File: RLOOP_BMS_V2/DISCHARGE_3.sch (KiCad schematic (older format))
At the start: 60 parts, among them Q2 PMV20ENR, Q3 PMV20ENR, Q4 PMV20ENR, Q5 PMV20ENR, Q6 PMV20ENR, Q7 PMV20ENR

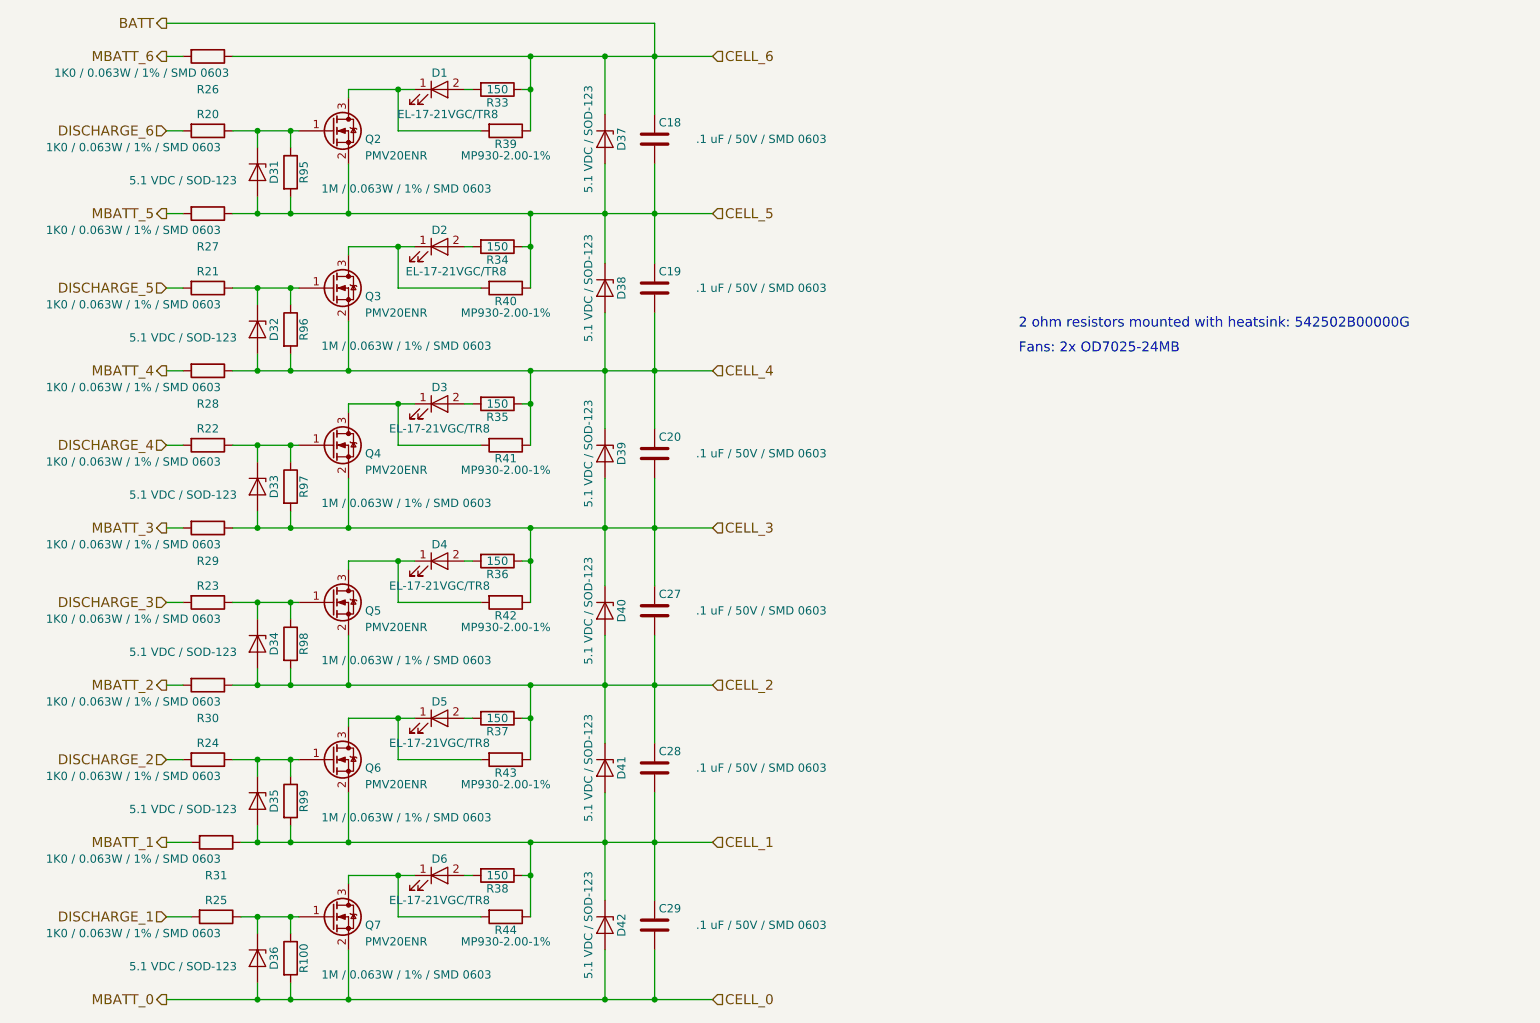
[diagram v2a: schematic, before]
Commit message: Added BOM, added pin 1 markings on a few parts
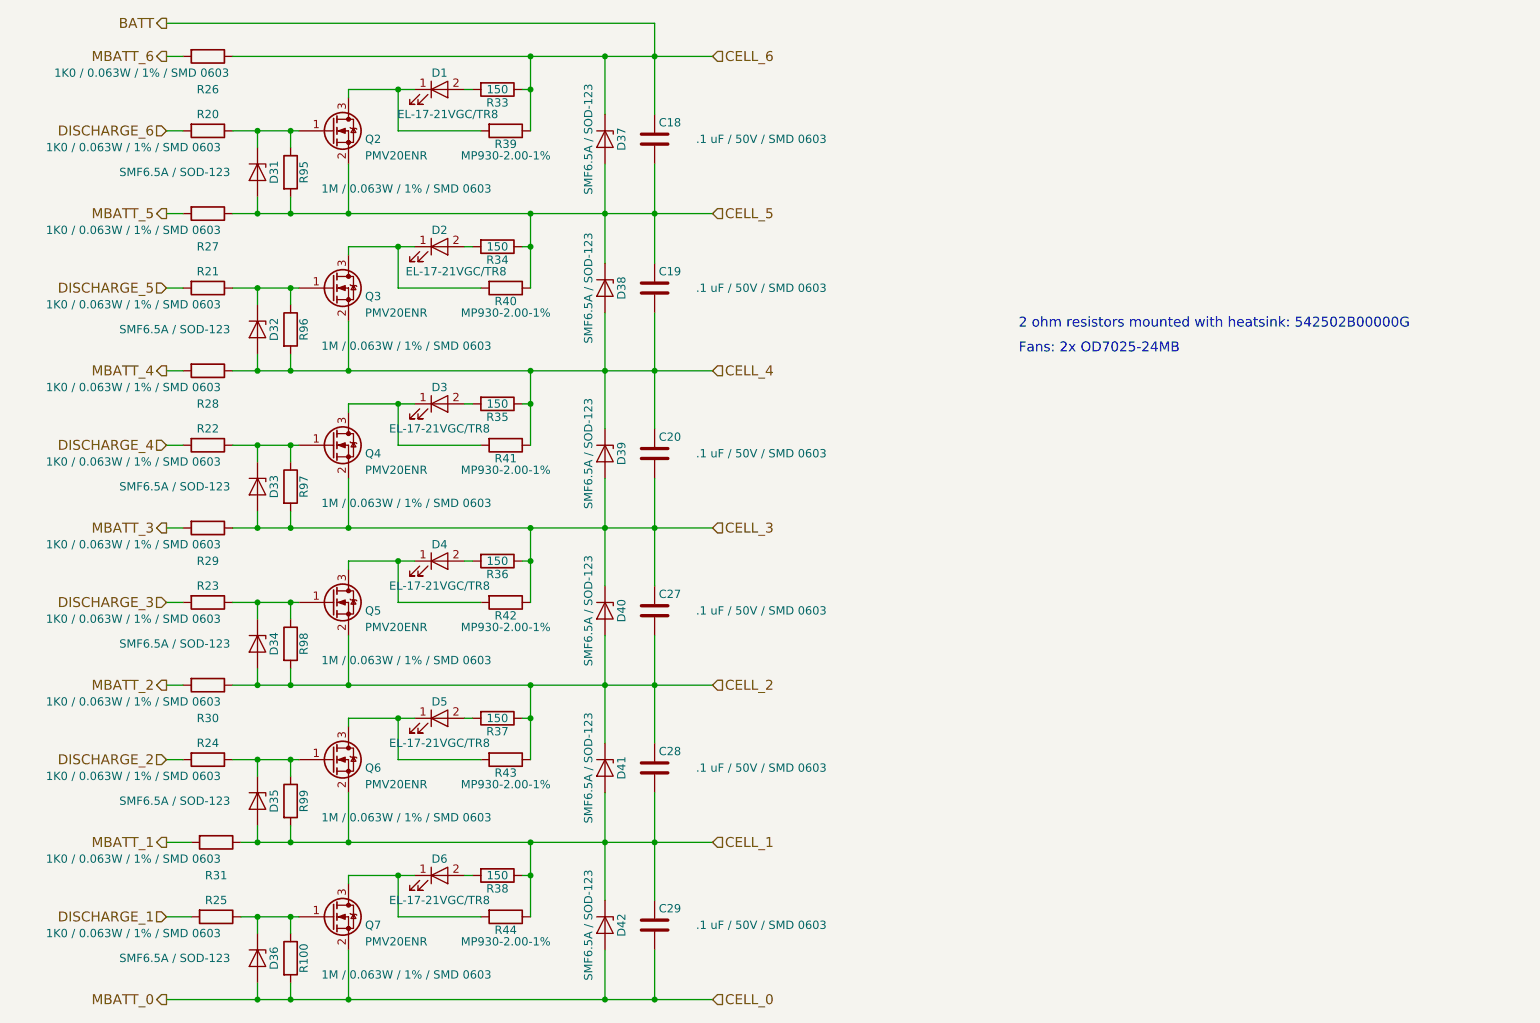
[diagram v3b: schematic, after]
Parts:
- D31, D32, D33, D34, D35, D36, D37, D38, D39, D40, D41, D42: value 5.1 VDC / SOD-123 -> SMF6.5A / SOD-123
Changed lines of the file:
@@
 P 4800 1750
 F 0 "D37" H 4800 1850 50  0000 C CNN
-F 1 "5.1 VDC / SOD-123" H 4800 1650 50  0000 C CNN
+F 1 "SMF6.5A / SOD-123" H 4800 1650 50  0000 C CNN
 F 2 "Diodes_SMD:D_SOD-123" H 4800 1750 50  0001 C CNN
 F 3 "" H 4800 1750 50  0001 C CNN
@@
 P 2700 1950
 F 0 "D31" H 2700 2050 50  0000 C CNN
-F 1 "5.1 VDC / SOD-123" V 2750 1500 50  0000 C CNN
+F 1 "SMF6.5A / SOD-123" V 2700 1450 50  0000 C CNN
 F 2 "Diodes_SMD:D_SOD-123" H 2700 1950 50  0001 C CNN
 F 3 "" H 2700 1950 50  0001 C CNN
@@
 P 4800 2650
 F 0 "D38" H 4800 2750 50  0000 C CNN
-F 1 "5.1 VDC / SOD-123" H 4800 2550 50  0000 C CNN
+F 1 "SMF6.5A / SOD-123" H 4800 2550 50  0000 C CNN
 F 2 "Diodes_SMD:D_SOD-123" H 4800 2650 50  0001 C CNN
 F 3 "" H 4800 2650 50  0001 C CNN
@@
 P 4800 3650
 F 0 "D39" H 4800 3750 50  0000 C CNN
-F 1 "5.1 VDC / SOD-123" H 4800 3550 50  0000 C CNN
+F 1 "SMF6.5A / SOD-123" H 4800 3550 50  0000 C CNN
 F 2 "Diodes_SMD:D_SOD-123" H 4800 3650 50  0001 C CNN
 F 3 "" H 4800 3650 50  0001 C CNN
@@
 P 4800 4600
 F 0 "D40" H 4800 4700 50  0000 C CNN
-F 1 "5.1 VDC / SOD-123" H 4800 4500 50  0000 C CNN
+F 1 "SMF6.5A / SOD-123" H 4800 4500 50  0000 C CNN
 F 2 "Diodes_SMD:D_SOD-123" H 4800 4600 50  0001 C CNN
 F 3 "" H 4800 4600 50  0001 C CNN
@@
 P 4800 5550
 F 0 "D41" H 4800 5650 50  0000 C CNN
-F 1 "5.1 VDC / SOD-123" H 4800 5450 50  0000 C CNN
+F 1 "SMF6.5A / SOD-123" H 4800 5450 50  0000 C CNN
 F 2 "Diodes_SMD:D_SOD-123" H 4800 5550 50  0001 C CNN
 F 3 "" H 4800 5550 50  0001 C CNN
@@
 P 4800 6500
 F 0 "D42" H 4800 6600 50  0000 C CNN
-F 1 "5.1 VDC / SOD-123" H 4800 6400 50  0000 C CNN
+F 1 "SMF6.5A / SOD-123" H 4800 6400 50  0000 C CNN
 F 2 "Diodes_SMD:D_SOD-123" H 4800 6500 50  0001 C CNN
 F 3 "" H 4800 6500 50  0001 C CNN
@@
 P 2700 2900
 F 0 "D32" H 2700 3000 50  0000 C CNN
-F 1 "5.1 VDC / SOD-123" V 2750 2450 50  0000 C CNN
+F 1 "SMF6.5A / SOD-123" V 2700 2400 50  0000 C CNN
 F 2 "Diodes_SMD:D_SOD-123" H 2700 2900 50  0001 C CNN
 F 3 "" H 2700 2900 50  0001 C CNN
@@
 P 2700 3850
 F 0 "D33" H 2700 3950 50  0000 C CNN
-F 1 "5.1 VDC / SOD-123" V 2750 3400 50  0000 C CNN
+F 1 "SMF6.5A / SOD-123" V 2700 3350 50  0000 C CNN
 F 2 "Diodes_SMD:D_SOD-123" H 2700 3850 50  0001 C CNN
 F 3 "" H 2700 3850 50  0001 C CNN
@@
 P 2700 4800
 F 0 "D34" H 2700 4900 50  0000 C CNN
-F 1 "5.1 VDC / SOD-123" V 2750 4350 50  0000 C CNN
+F 1 "SMF6.5A / SOD-123" V 2700 4300 50  0000 C CNN
 F 2 "Diodes_SMD:D_SOD-123" H 2700 4800 50  0001 C CNN
 F 3 "" H 2700 4800 50  0001 C CNN
@@
 P 2700 5750
 F 0 "D35" H 2700 5850 50  0000 C CNN
-F 1 "5.1 VDC / SOD-123" V 2750 5300 50  0000 C CNN
+F 1 "SMF6.5A / SOD-123" V 2700 5250 50  0000 C CNN
 F 2 "Diodes_SMD:D_SOD-123" H 2700 5750 50  0001 C CNN
 F 3 "" H 2700 5750 50  0001 C CNN
@@
 P 2700 6700
 F 0 "D36" H 2700 6800 50  0000 C CNN
-F 1 "5.1 VDC / SOD-123" V 2750 6250 50  0000 C CNN
+F 1 "SMF6.5A / SOD-123" V 2700 6200 50  0000 C CNN
 F 2 "Diodes_SMD:D_SOD-123" H 2700 6700 50  0001 C CNN
 F 3 "" H 2700 6700 50  0001 C CNN

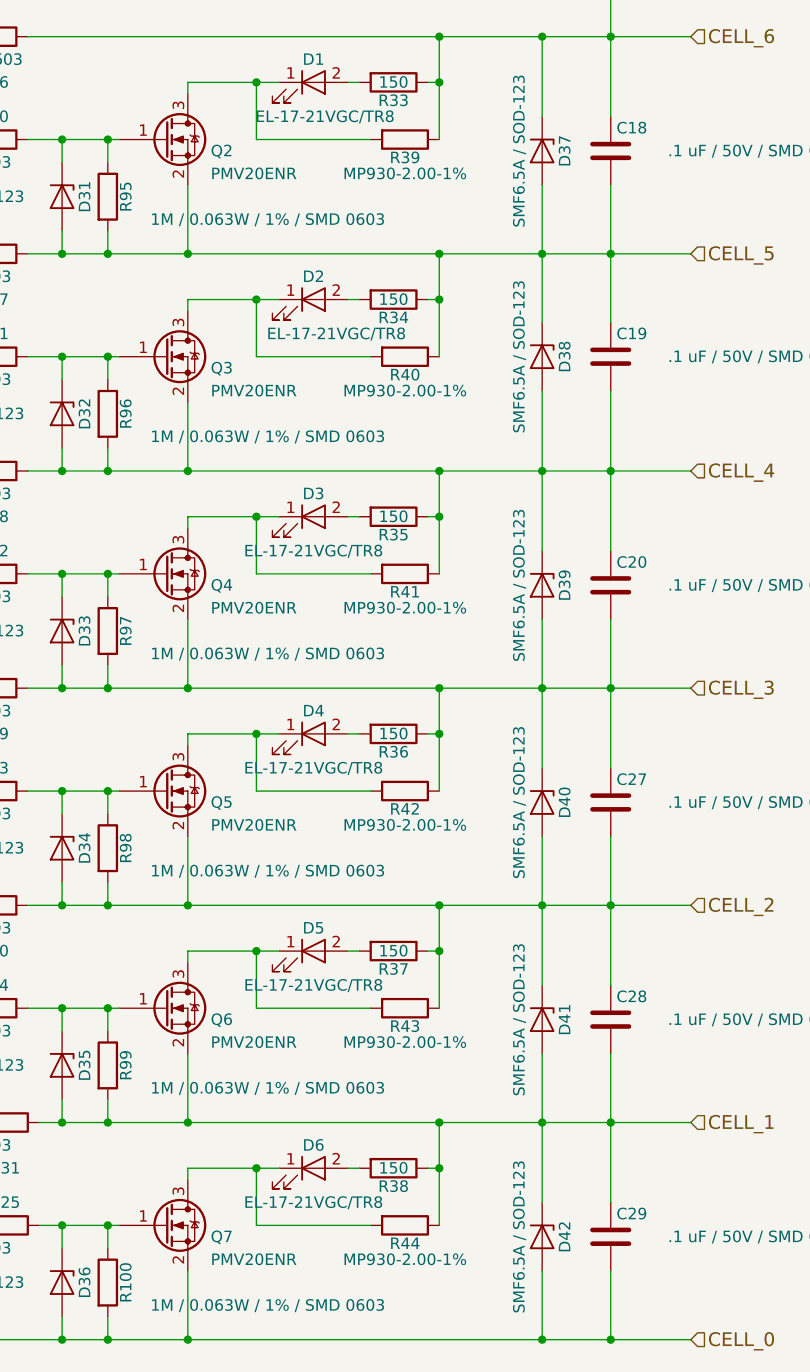
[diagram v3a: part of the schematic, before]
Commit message: Change 2 Ohm Resistor
Had to change for heatsink mounting :/
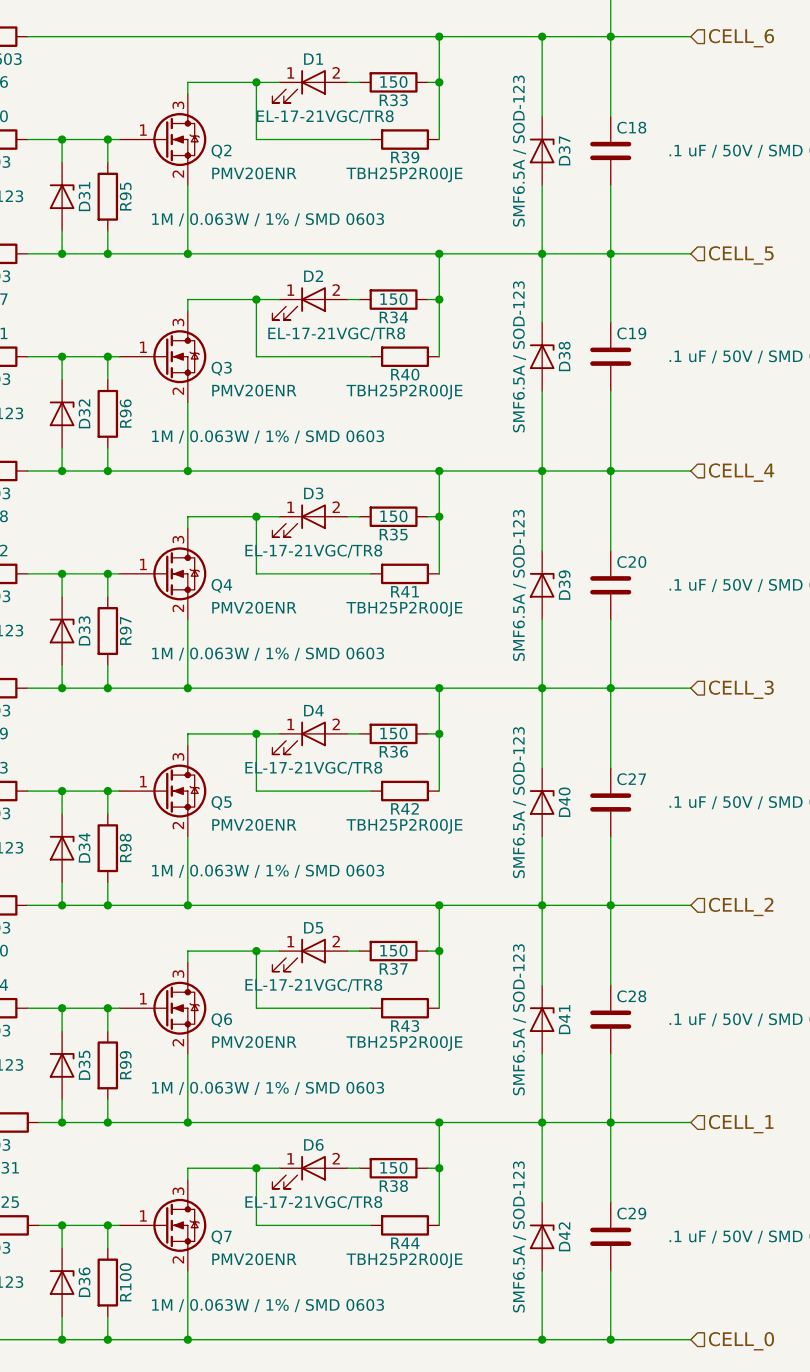
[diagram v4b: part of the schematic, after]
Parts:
- R39, R40, R41, R42, R43, R44: value MP930-2.00-1% -> TBH25P2R00JE
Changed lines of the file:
@@
 P 4200 1700
 F 0 "R39" V 4280 1700 50  0000 C CNN
-F 1 "MP930-2.00-1%" V 4350 1700 50  0000 C CNN
+F 1 "TBH25P2R00JE" V 4350 1700 50  0000 C CNN
 F 2 "rLoop_Footprints:Res_MP930" V 4130 1700 50  0001 C CNN
 F 3 "" H 4200 1700 50  0001 C CNN
@@
 P 4200 2650
 F 0 "R40" V 4280 2650 50  0000 C CNN
-F 1 "MP930-2.00-1%" V 4350 2650 50  0000 C CNN
+F 1 "TBH25P2R00JE" V 4350 2650 50  0000 C CNN
 F 2 "rLoop_Footprints:Res_MP930" V 4130 2650 50  0001 C CNN
 F 3 "" H 4200 2650 50  0001 C CNN
@@
 P 4200 3600
 F 0 "R41" V 4280 3600 50  0000 C CNN
-F 1 "MP930-2.00-1%" V 4350 3600 50  0000 C CNN
+F 1 "TBH25P2R00JE" V 4350 3600 50  0000 C CNN
 F 2 "rLoop_Footprints:Res_MP930" V 4130 3600 50  0001 C CNN
 F 3 "" H 4200 3600 50  0001 C CNN
@@
 P 4200 4550
 F 0 "R42" V 4280 4550 50  0000 C CNN
-F 1 "MP930-2.00-1%" V 4350 4550 50  0000 C CNN
+F 1 "TBH25P2R00JE" V 4350 4550 50  0000 C CNN
 F 2 "rLoop_Footprints:Res_MP930" V 4130 4550 50  0001 C CNN
 F 3 "" H 4200 4550 50  0001 C CNN
@@
 P 4200 5500
 F 0 "R43" V 4280 5500 50  0000 C CNN
-F 1 "MP930-2.00-1%" V 4350 5500 50  0000 C CNN
+F 1 "TBH25P2R00JE" V 4350 5500 50  0000 C CNN
 F 2 "rLoop_Footprints:Res_MP930" V 4130 5500 50  0001 C CNN
 F 3 "" H 4200 5500 50  0001 C CNN
@@
 P 4200 6450
 F 0 "R44" V 4280 6450 50  0000 C CNN
-F 1 "MP930-2.00-1%" V 4350 6450 50  0000 C CNN
+F 1 "TBH25P2R00JE" V 4350 6450 50  0000 C CNN
 F 2 "rLoop_Footprints:Res_MP930" V 4130 6450 50  0001 C CNN
 F 3 "" H 4200 6450 50  0001 C CNN

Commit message: swapped a few connectors to standardize with the power node and what's readily available
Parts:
- R39, R40, R41, R42, R43, R44: footprint rLoop_Footprints:Res_MP930 -> rLoop_Footprints:2-OHM-TO-220-TBH25P2R00JE
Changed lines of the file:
@@
 F 0 "R39" V 4280 1700 50  0000 C CNN
 F 1 "TBH25P2R00JE" V 4350 1700 50  0000 C CNN
-F 2 "rLoop_Footprints:Res_MP930" V 4130 1700 50  0001 C CNN
+F 2 "rLoop_Footprints:2-OHM-TO-220-TBH25P2R00JE" V 4130 1700 50  0001 C CNN
 F 3 "" H 4200 1700 50  0001 C CNN
 	1    4200 1700
@@
 F 0 "R40" V 4280 2650 50  0000 C CNN
 F 1 "TBH25P2R00JE" V 4350 2650 50  0000 C CNN
-F 2 "rLoop_Footprints:Res_MP930" V 4130 2650 50  0001 C CNN
+F 2 "rLoop_Footprints:2-OHM-TO-220-TBH25P2R00JE" V 4130 2650 50  0001 C CNN
 F 3 "" H 4200 2650 50  0001 C CNN
 	1    4200 2650
@@
 F 0 "R41" V 4280 3600 50  0000 C CNN
 F 1 "TBH25P2R00JE" V 4350 3600 50  0000 C CNN
-F 2 "rLoop_Footprints:Res_MP930" V 4130 3600 50  0001 C CNN
+F 2 "rLoop_Footprints:2-OHM-TO-220-TBH25P2R00JE" V 4130 3600 50  0001 C CNN
 F 3 "" H 4200 3600 50  0001 C CNN
 	1    4200 3600
@@
 F 0 "R42" V 4280 4550 50  0000 C CNN
 F 1 "TBH25P2R00JE" V 4350 4550 50  0000 C CNN
-F 2 "rLoop_Footprints:Res_MP930" V 4130 4550 50  0001 C CNN
+F 2 "rLoop_Footprints:2-OHM-TO-220-TBH25P2R00JE" V 4130 4550 50  0001 C CNN
 F 3 "" H 4200 4550 50  0001 C CNN
 	1    4200 4550
@@
 F 0 "R43" V 4280 5500 50  0000 C CNN
 F 1 "TBH25P2R00JE" V 4350 5500 50  0000 C CNN
-F 2 "rLoop_Footprints:Res_MP930" V 4130 5500 50  0001 C CNN
+F 2 "rLoop_Footprints:2-OHM-TO-220-TBH25P2R00JE" V 4130 5500 50  0001 C CNN
 F 3 "" H 4200 5500 50  0001 C CNN
 	1    4200 5500
@@
 F 0 "R44" V 4280 6450 50  0000 C CNN
 F 1 "TBH25P2R00JE" V 4350 6450 50  0000 C CNN
-F 2 "rLoop_Footprints:Res_MP930" V 4130 6450 50  0001 C CNN
+F 2 "rLoop_Footprints:2-OHM-TO-220-TBH25P2R00JE" V 4130 6450 50  0001 C CNN
 F 3 "" H 4200 6450 50  0001 C CNN
 	1    4200 6450
